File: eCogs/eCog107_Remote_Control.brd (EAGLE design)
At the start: 47.5 x 28 mm, 11 parts, among them T1 MMBT3904LT1G, T3 MMBT3904LT1G, U1 PNA460XM

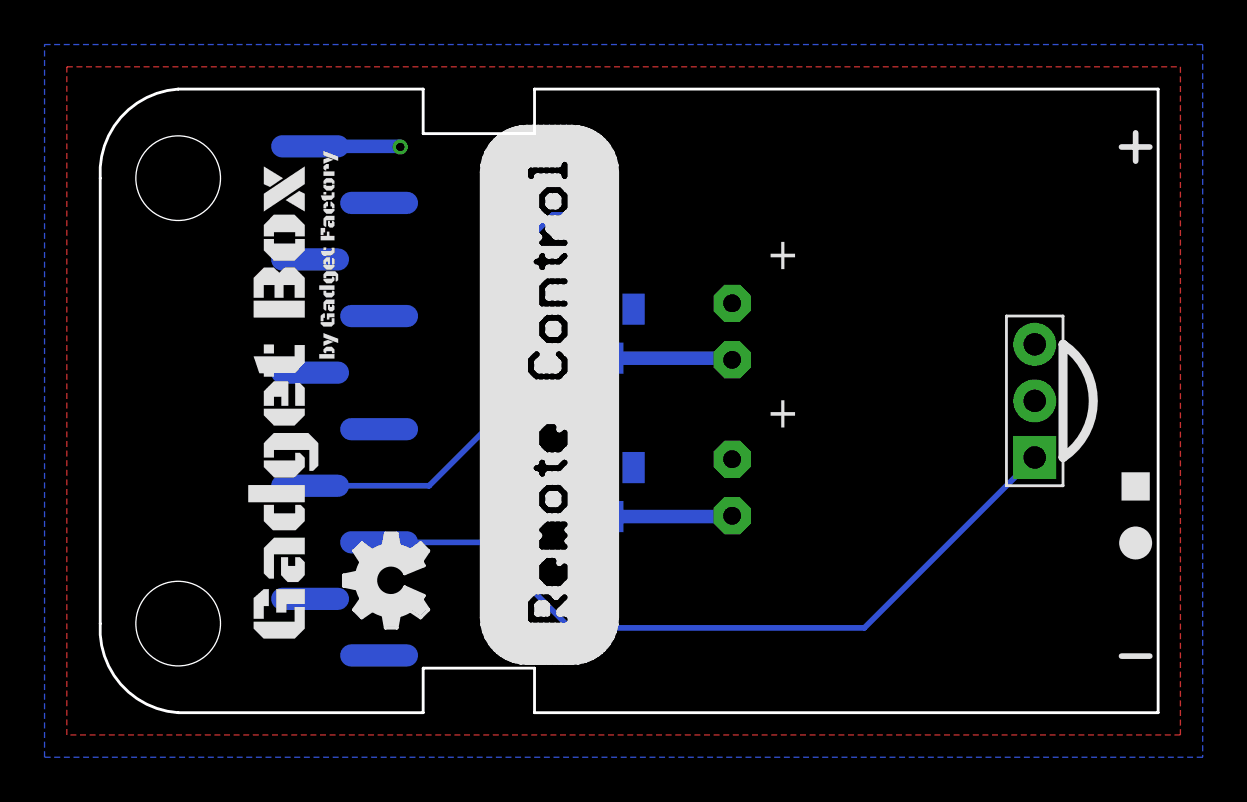
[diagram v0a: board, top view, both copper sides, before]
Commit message: Update Remote Control Design
Put the transmit PWM pin on XC4 for greater compatibility.
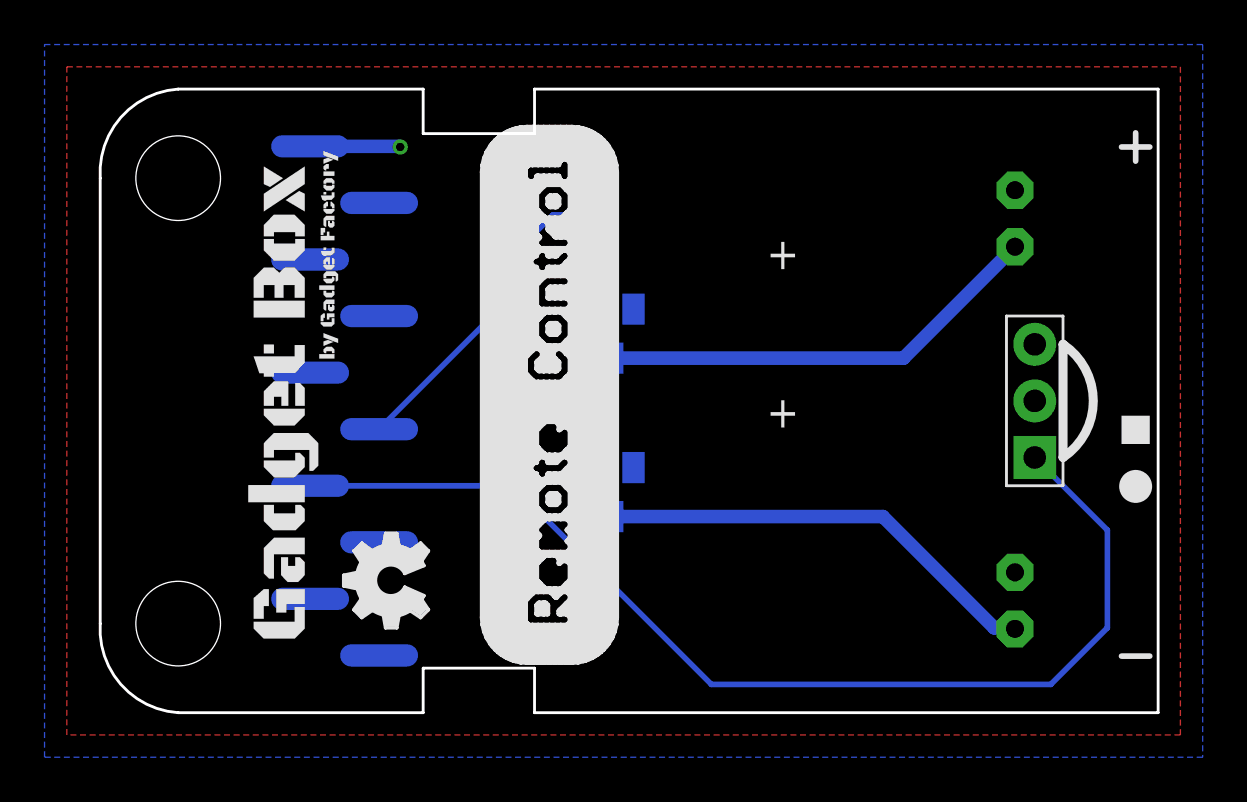
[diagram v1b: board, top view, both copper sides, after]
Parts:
- removed U$4: (no value), eCogs:LEGEND_DIO
- added U$1: (no value), eCogs:LEGEND_PWM
- U$2: device eCogs:LEGEND_PWM -> eCogs:LEGEND_DIO
- moved IR1 13.7 mm to (41.6, 5.03)
- moved IR2 13.7 mm to (41.6, 22.2)
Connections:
- removed net BLAST_RX: ECOG.G0
- removed net BLAST_TX: ECOG.G3
- net RECEIVE: now also ECOG.G2; no longer ECOG.G1
- net TRANSMIT: now also ECOG.G3; no longer ECOG.G2
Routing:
- net RECEIVE: track 34.2 -> 49.5 mm
- net N$7: track 5.39 -> 20.2 mm
- net N$9: track 5.41 -> 20.2 mm
- net TRANSMIT: track 21.6 -> 14.7 mm
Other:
- board text added: "XC2"
- board text added: "XC3"
- board text added: "ecog107 v2.1"
- board text removed: "1"
- board text removed: "2"
- board text removed: "ecog107 v2.0"
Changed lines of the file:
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@@
 <board>
 <plain>
-<text x="39.045" y="22.559" size="0.8128" layer="22" font="vector" rot="MR270">ecog107.GadgetFactory.net</text>
-<text x="36.301" y="19.702" size="1.016" layer="22" font="vector" rot="MR270">ecog107 v2.0</text>
-<text x="35.031" y="19.702" size="1.016" layer="22" font="vector" rot="MR270">Remote Control</text>
-<text x="33.761" y="19.702" size="1.016" layer="22" font="vector" rot="MR270">eCogs</text>
-<text x="22.495" y="7.112" size="1.016" layer="22" font="vector" rot="MR0">RECEIVE</text>
-<text x="20.875" y="9.652" size="1.016" layer="22" font="vector" rot="MR0">TRANSMIT</text>
-<text x="39.934" y="18.782" size="0.6096" layer="22" font="vector" rot="MR270">Copyright 2016</text>
-<text x="40.823" y="20.512" size="0.6096" layer="22" font="vector" rot="MR270">Gadget Factory, LLC</text>
+<text x="33.965" y="22.559" size="0.8128" layer="22" font="vector" rot="MR270">ecog107.GadgetFactory.net</text>
+<text x="31.221" y="19.702" size="1.016" layer="22" font="vector" rot="MR270">ecog107 v2.1</text>
+<text x="29.951" y="19.702" size="1.016" layer="22" font="vector" rot="MR270">Remote Control</text>
+<text x="28.681" y="19.702" size="1.016" layer="22" font="vector" rot="MR270">eCogs</text>
+<text x="19.955" y="9.652" size="1.016" layer="22" font="vector" rot="MR0">RECEIVE</text>
+<text x="22.145" y="12.192" size="1.016" layer="22" font="vector" rot="MR0">TRANSMIT</text>
+<text x="34.854" y="18.782" size="0.6096" layer="22" font="vector" rot="MR270">Copyright 2016</text>
+<text x="35.743" y="20.512" size="0.6096" layer="22" font="vector" rot="MR270">Gadget Factory, LLC</text>
 <text x="17.431" y="24.511" size="1.016" layer="22" font="vector" rot="MR0">3.3V</text>
 <text x="17.587" y="2.567" size="1.016" layer="22" font="vector" rot="MR0">GND</text>
@@
 <wire x1="46.355" y1="25.4" x2="47.625" y2="25.4" width="0.254" layer="21"/>
 <wire x1="46.355" y1="2.54" x2="47.625" y2="2.54" width="0.254" layer="21"/>
-<text x="9.205" y="7.012" size="1.016" layer="22" font="vector" rot="MR0">1</text>
-<text x="6.665" y="9.552" size="1.016" layer="22" font="vector" rot="MR0">2</text>
+<text x="6.665" y="9.552" size="1.016" layer="22" font="vector" rot="MR0">XC2</text>
+<text x="6.665" y="12.092" size="1.016" layer="22" font="vector" rot="MR0">XC3</text>
 </plain>
 <attributes>
@@
 <attribute name="DIGIKEY" value="S1013EC-10-ND" x="0" y="0" size="1.778" layer="27" display="off"/>
 </element>
-<element name="U$4" library="eCogs" package="LEGEND_DIO" value="" x="46.99" y="7.62"/>
-<element name="U$2" library="eCogs" package="LEGEND_PWM" value="" x="46.99" y="10.16"/>
 <element name="R1" library="rcl-ez" package="R0805" value="1.0 K" x="22.622" y="21.543" smashed="yes" rot="MR270">
 <attribute name="NAME" x="24.862" y="22.679" size="1.27" layer="26" font="vector" ratio="10" rot="MR270"/>
@@
 <element name="U1" library="adafruit" package="PNA460XM" value="PNA460XM" x="42.46" y="14" smashed="yes" rot="R90">
 <attribute name="DIGIKEY" value="751-1227-ND" x="42.46" y="14" size="1.778" layer="27" rot="R90" display="off"/>
-<attribute name="NAME" x="42.0888" y="7.1138" size="1.27" layer="26" ratio="10" rot="MR90"/>
+<attribute name="NAME" x="45.8988" y="13.4638" size="1.27" layer="26" ratio="10" rot="MR90"/>
 </element>
 <element name="T1" library="transistor" package="SOT23-BEC" value="MMBT3904LT1G" x="23.495" y="9.906" smashed="yes" rot="MR180">
@@
 <attribute name="VALUE" x="21.59" y="20.193" size="1.27" layer="28" rot="MR180"/>
 </element>
-<element name="IR1" library="adafruit" package="LED5MM" value="" x="28.873" y="10.112" smashed="yes" rot="R270">
-<attribute name="NAME" x="33.2396" y="12.737" size="1.27" layer="26" ratio="10" rot="MR270"/>
-<attribute name="VALUE" x="27.0696" y="6.9116" size="1.27" layer="27" ratio="10" rot="R270"/>
-<attribute name="DIGIKEY" value="1080-1082-ND" x="28.873" y="10.112" size="1.778" layer="27" rot="R270" display="off"/>
+<element name="IR1" library="adafruit" package="LED5MM" value="" x="41.573" y="5.032" smashed="yes" rot="R270">
+<attribute name="NAME" x="45.9396" y="7.657" size="1.27" layer="26" ratio="10" rot="MR270"/>
+<attribute name="VALUE" x="39.7696" y="1.8316" size="1.27" layer="27" ratio="10" rot="R270"/>
+<attribute name="DIGIKEY" value="1080-1082-ND" x="41.573" y="5.032" size="1.778" layer="27" rot="R270" display="off"/>
 </element>
-<element name="IR2" library="adafruit" package="LED5MM" value="" x="28.873" y="17.112" smashed="yes" rot="R270">
-<attribute name="NAME" x="33.2396" y="19.737" size="1.27" layer="26" ratio="10" rot="MR270"/>
-<attribute name="VALUE" x="27.0696" y="13.9116" size="1.27" layer="27" ratio="10" rot="R270"/>
-<attribute name="DIGIKEY" value="1080-1080-ND" x="28.873" y="17.112" size="1.778" layer="27" rot="R270" display="off"/>
+<element name="IR2" library="adafruit" package="LED5MM" value="" x="41.573" y="22.192" smashed="yes" rot="R270">
+<attribute name="NAME" x="45.9396" y="24.817" size="1.27" layer="26" ratio="10" rot="MR270"/>
+<attribute name="VALUE" x="39.7696" y="18.9916" size="1.27" layer="27" ratio="10" rot="R270"/>
+<attribute name="DIGIKEY" value="1080-1080-ND" x="41.573" y="22.192" size="1.778" layer="27" rot="R270" display="off"/>
 </element>
 <element name="U$5" library="GadgetFactory" package="GADGETBOX_SMALL" value="" x="8.79" y="14" rot="R90"/>
 <element name="U$6" library="ohw-logo" package="OSHW_FILLX150_NOTEXT" value="" x="15.24" y="3.81" rot="R90"/>
+<element name="U$1" library="eCogs" package="LEGEND_PWM" value="" x="46.99" y="12.7"/>
+<element name="U$2" library="eCogs" package="LEGEND_DIO" value="" x="46.99" y="10.16"/>
 </elements>
 <signals>
@@
 <contactref element="T3" pad="C"/>
 <contactref element="IR2" pad="K"/>
-<wire x1="23.495" y1="15.918" x2="28.797" y2="15.918" width="0.6096" layer="16"/>
-<wire x1="28.797" y1="15.918" x2="28.873" y2="15.842" width="0.6096" layer="16"/>
+<wire x1="23.495" y1="15.918" x2="36.569" y2="15.918" width="0.6096" layer="16"/>
+<wire x1="36.569" y1="15.918" x2="41.573" y2="20.922" width="0.6096" layer="16"/>
 </signal>
 <signal name="TRANSMIT">
-<contactref element="ECOG" pad="G2"/>
 <contactref element="R1" pad="1"/>
-<wire x1="9.92324375" y1="10.189" x2="15.269" y2="10.189" width="0.254" layer="16"/>
-<wire x1="15.269" y1="10.189" x2="19.05" y2="13.97" width="0.254" layer="16"/>
-<wire x1="19.05" y1="13.97" x2="19.05" y2="20.574" width="0.254" layer="16"/>
 <wire x1="19.05" y1="20.574" x2="20.828" y2="22.352" width="0.254" layer="16"/>
 <wire x1="20.828" y1="22.352" x2="22.581" y2="22.352" width="0.254" layer="16"/>
 <wire x1="22.581" y1="22.352" x2="22.622" y2="22.393" width="0.254" layer="16"/>
+<contactref element="ECOG" pad="G3"/>
+<wire x1="19.05" y1="20.574" x2="19.05" y2="18.75695625" width="0.254" layer="16"/>
+<wire x1="19.05" y1="18.75695625" x2="13.02204375" y2="12.729" width="0.254" layer="16"/>
 </signal>
 <signal name="N$7">
 <contactref element="T1" pad="C"/>
 <contactref element="IR1" pad="K"/>
-<wire x1="23.495" y1="8.806" x2="28.837" y2="8.806" width="0.6096" layer="16"/>
-<wire x1="28.837" y1="8.806" x2="28.873" y2="8.842" width="0.6096" layer="16"/>
+<wire x1="23.495" y1="8.806" x2="35.644" y2="8.806" width="0.6096" layer="16"/>
+<wire x1="35.644" y1="8.806" x2="40.64" y2="3.81" width="0.6096" layer="16"/>
+<wire x1="40.64" y1="3.81" x2="41.525" y2="3.81" width="0.6096" layer="16"/>
+<wire x1="41.525" y1="3.81" x2="41.573" y2="3.762" width="0.6096" layer="16"/>
 </signal>
 <signal name="N$10">
@@
 </signal>
 <signal name="RECEIVE">
-<contactref element="ECOG" pad="G1"/>
 <contactref element="U1" pad="1"/>
-<wire x1="13.02204375" y1="7.649" x2="17.751" y2="7.649" width="0.254" layer="16"/>
-<wire x1="17.751" y1="7.649" x2="21.59" y2="3.81" width="0.254" layer="16"/>
-<wire x1="21.59" y1="3.81" x2="34.81" y2="3.81" width="0.254" layer="16"/>
-<wire x1="34.81" y1="3.81" x2="42.46" y2="11.46" width="0.254" layer="16"/>
-</signal>
-<signal name="BLAST_RX">
-<contactref element="ECOG" pad="G0"/>
-</signal>
-<signal name="BLAST_TX">
-<contactref element="ECOG" pad="G3"/>
+<contactref element="ECOG" pad="G2"/>
+<wire x1="9.92324375" y1="10.189" x2="19.021" y2="10.189" width="0.254" layer="16"/>
+<wire x1="19.021" y1="10.189" x2="27.94" y2="1.27" width="0.254" layer="16"/>
+<wire x1="27.94" y1="1.27" x2="43.18" y2="1.27" width="0.254" layer="16"/>
+<wire x1="43.18" y1="1.27" x2="45.72" y2="3.81" width="0.254" layer="16"/>
+<wire x1="45.72" y1="3.81" x2="45.72" y2="8.2" width="0.254" layer="16"/>
+<wire x1="45.72" y1="8.2" x2="42.46" y2="11.46" width="0.254" layer="16"/>
 </signal>
 </signals>

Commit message: Updated to latest eCog Library
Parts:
- ECOG: value ECOG_GENERAL_ROWECOG_GENERAL_SMD -> ECOG_GENERAL_ROWSURFACEMOUNT
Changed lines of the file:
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@@
 </autorouter>
 <elements>
-<element name="ECOG" library="eCogs" package="ECOG_GENERAL_SMD" value="ECOG_GENERAL_ROWECOG_GENERAL_SMD" x="0" y="0" smashed="yes">
+<element name="ECOG" library="eCogs" package="ECOG_GENERAL_SMD" value="ECOG_GENERAL_ROWSURFACEMOUNT" x="0" y="0" smashed="yes">
 <attribute name="DIGIKEY" value="S1013EC-10-ND" x="0" y="0" size="1.778" layer="27" display="off"/>
 </element>
